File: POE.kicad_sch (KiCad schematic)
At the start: 9 parts, among them J1 Conn_01x02_Male

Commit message: ...
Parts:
- MOD-1: Footprint_1 Ag9912LP -> (none); Manufacturer_Part_Number Ag9912LP -> Ag9905LP; Mouser Part Number 480-AG9912LP -> (none); Mouser Price/Stock https://www.mouser.co.uk/ProductDetail/Silvertel/Ag9912LP?q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 -> (none); Reference_1 IC -> (none); Value_1 Ag9905LP -> (none)
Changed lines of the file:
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@@
       (effects (font (size 1.27 1.27)) hide)
-    )
-    (property "Reference_1" "IC" (id 4) (at 237.49 43.18 0))
-    (property "Value_1" "Ag9905LP" (id 5) (at 237.49 45.72 0))
-    (property "Footprint_1" "Ag9912LP" (id 6) (at 250.19 145.72 0)
-      (effects (font (size 1.27 1.27)) (justify left top) hide)
     )
     (property "Datasheet_1" "https://au.mouser.com/datasheet/2/1048/Ag9900M-datasheet-ultra-miniature-isolated-Power-o-1804309.pdf" (id 7) (at 250.19 245.72 0)
@@
       (effects (font (size 1.27 1.27)) (justify left top) hide)
     )
-    (property "Manufacturer_Part_Number" "Ag9912LP" (id 10) (at 250.19 645.72 0)
+    (property "Manufacturer_Part_Number" "Ag9905LP" (id 10) (at 250.19 645.72 0)
       (effects (font (size 1.27 1.27)) (justify left top) hide)
     )
-    (property "Mouser Part Number" "480-AG9912LP" (id 11) (at 250.19 745.72 0)
-      (effects (font (size 1.27 1.27)) (justify left top) hide)
-    )
-    (property "Mouser Price/Stock" "https://www.mouser.co.uk/ProductDetail/Silvertel/Ag9912LP?qs=OlC7AqGiEDllGSVQiYaPRA%3D%3D" (id 12) (at 250.19 845.72 0)
-      (effects (font (size 1.27 1.27)) (justify left top) hide)
-    )
-    (property "Arrow Part Number" "" (id 13) (at 250.19 945.72 0)
-      (effects (font (size 1.27 1.27)) (justify left top) hide)
-    )
-    (property "Arrow Price/Stock" "" (id 14) (at 250.19 1045.72 0)
-      (effects (font (size 1.27 1.27)) (justify left top) hide)
-    )

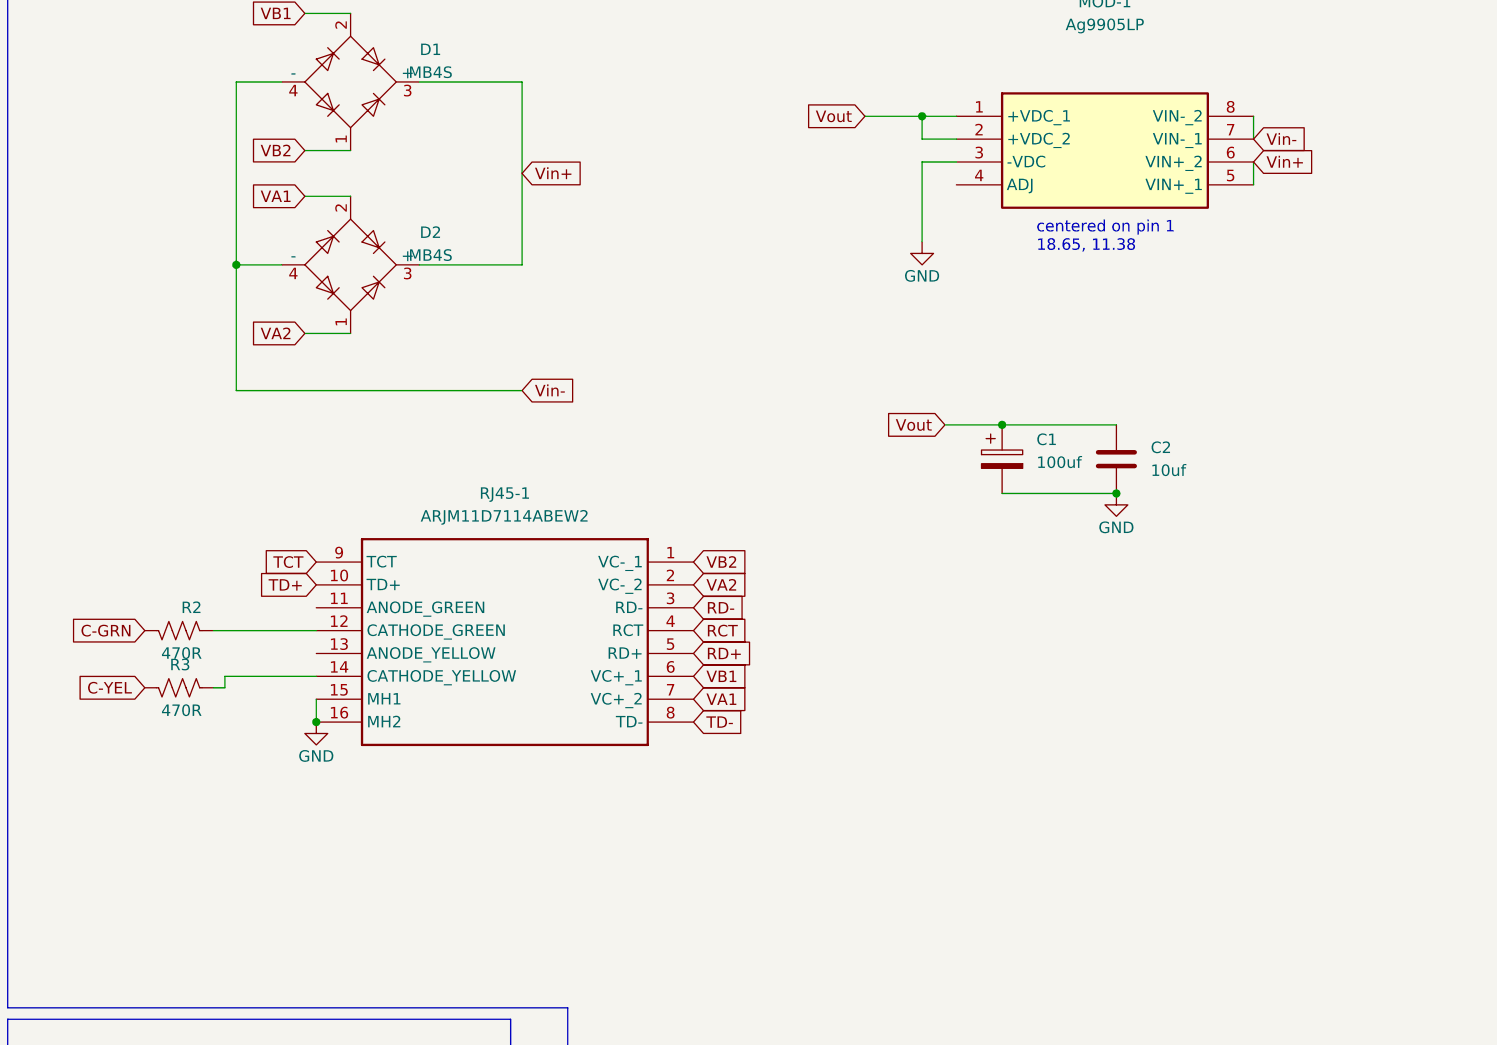
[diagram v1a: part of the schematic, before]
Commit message: Added adjustment & minLoad resistors
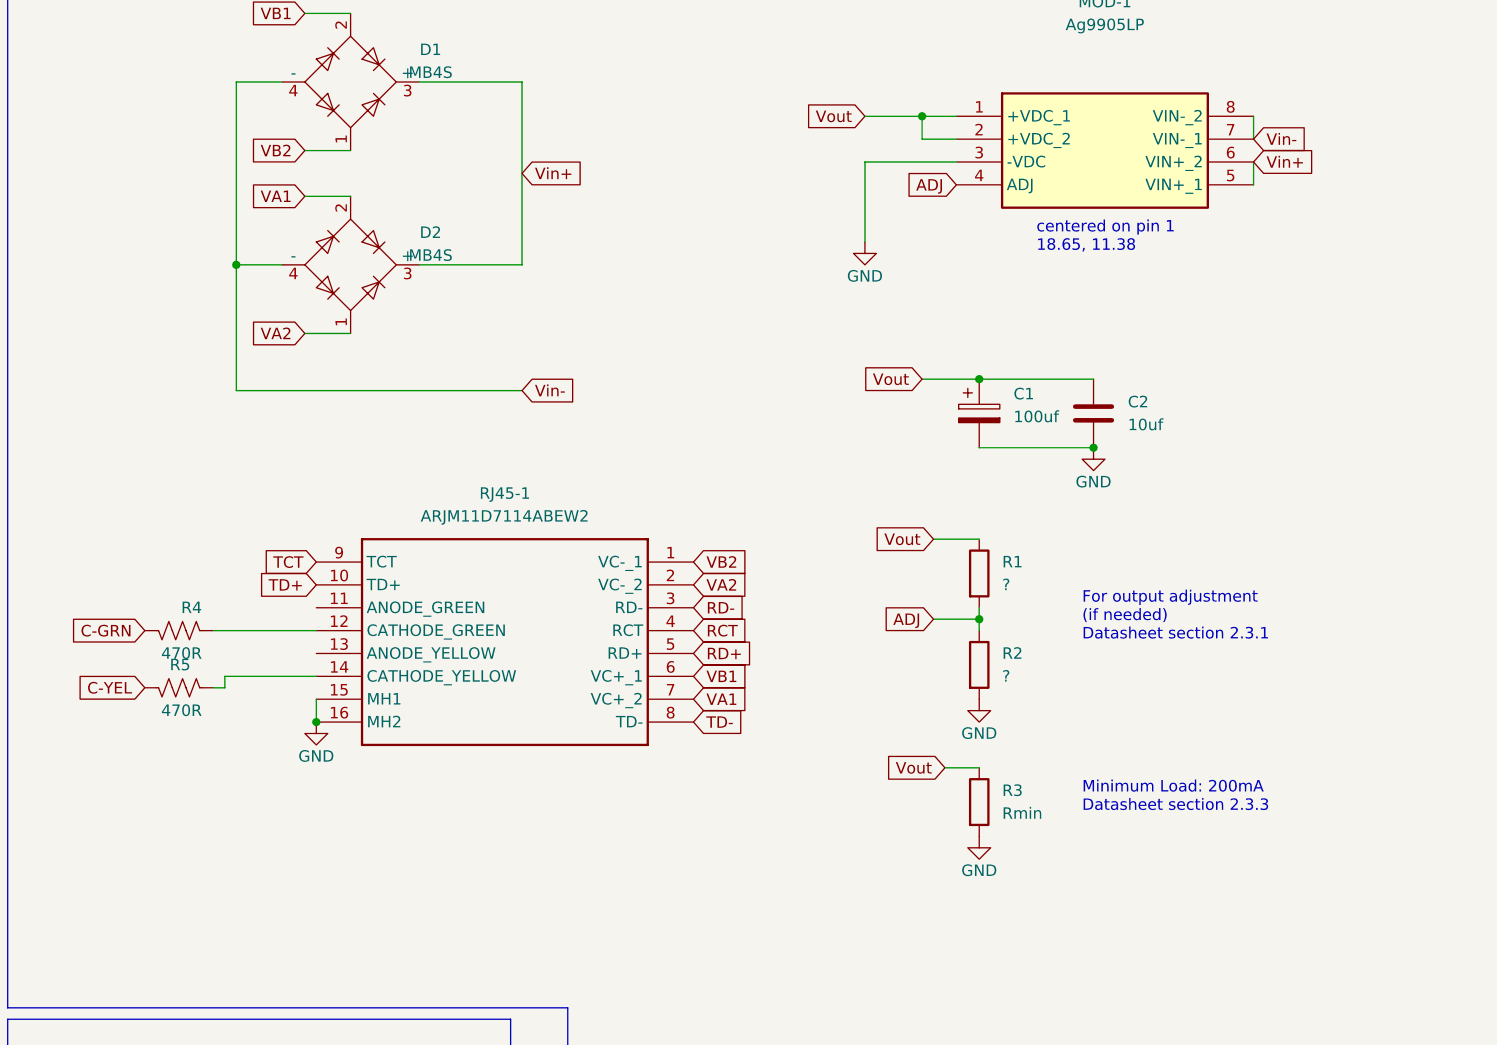
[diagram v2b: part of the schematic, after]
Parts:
- added R1, R2: ?, Resistor_SMD:R_0805_2012Metric_Pad1.20x1.40mm_HandSolder, symbol Device:R
- added R3: Rmin, Resistor_SMD:R_0805_2012Metric_Pad1.20x1.40mm_HandSolder, symbol Device:R
- renumbered R2 to R4, R3 to R5
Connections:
- net GND: now also R2.2, R3.2
- net Vout: now also R1.1, R3.1
- net ADJ: now reaches MOD-1.4 (ADJ)
- net ADJ: now also R1.2, R2.1
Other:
- note added: "For output adjustment (if needed) Datasheet section 2.3.1"
- note added: "Minimum Load: 200mA Datasheet section 2.3.3"
- moved on the sheet: C1, C2

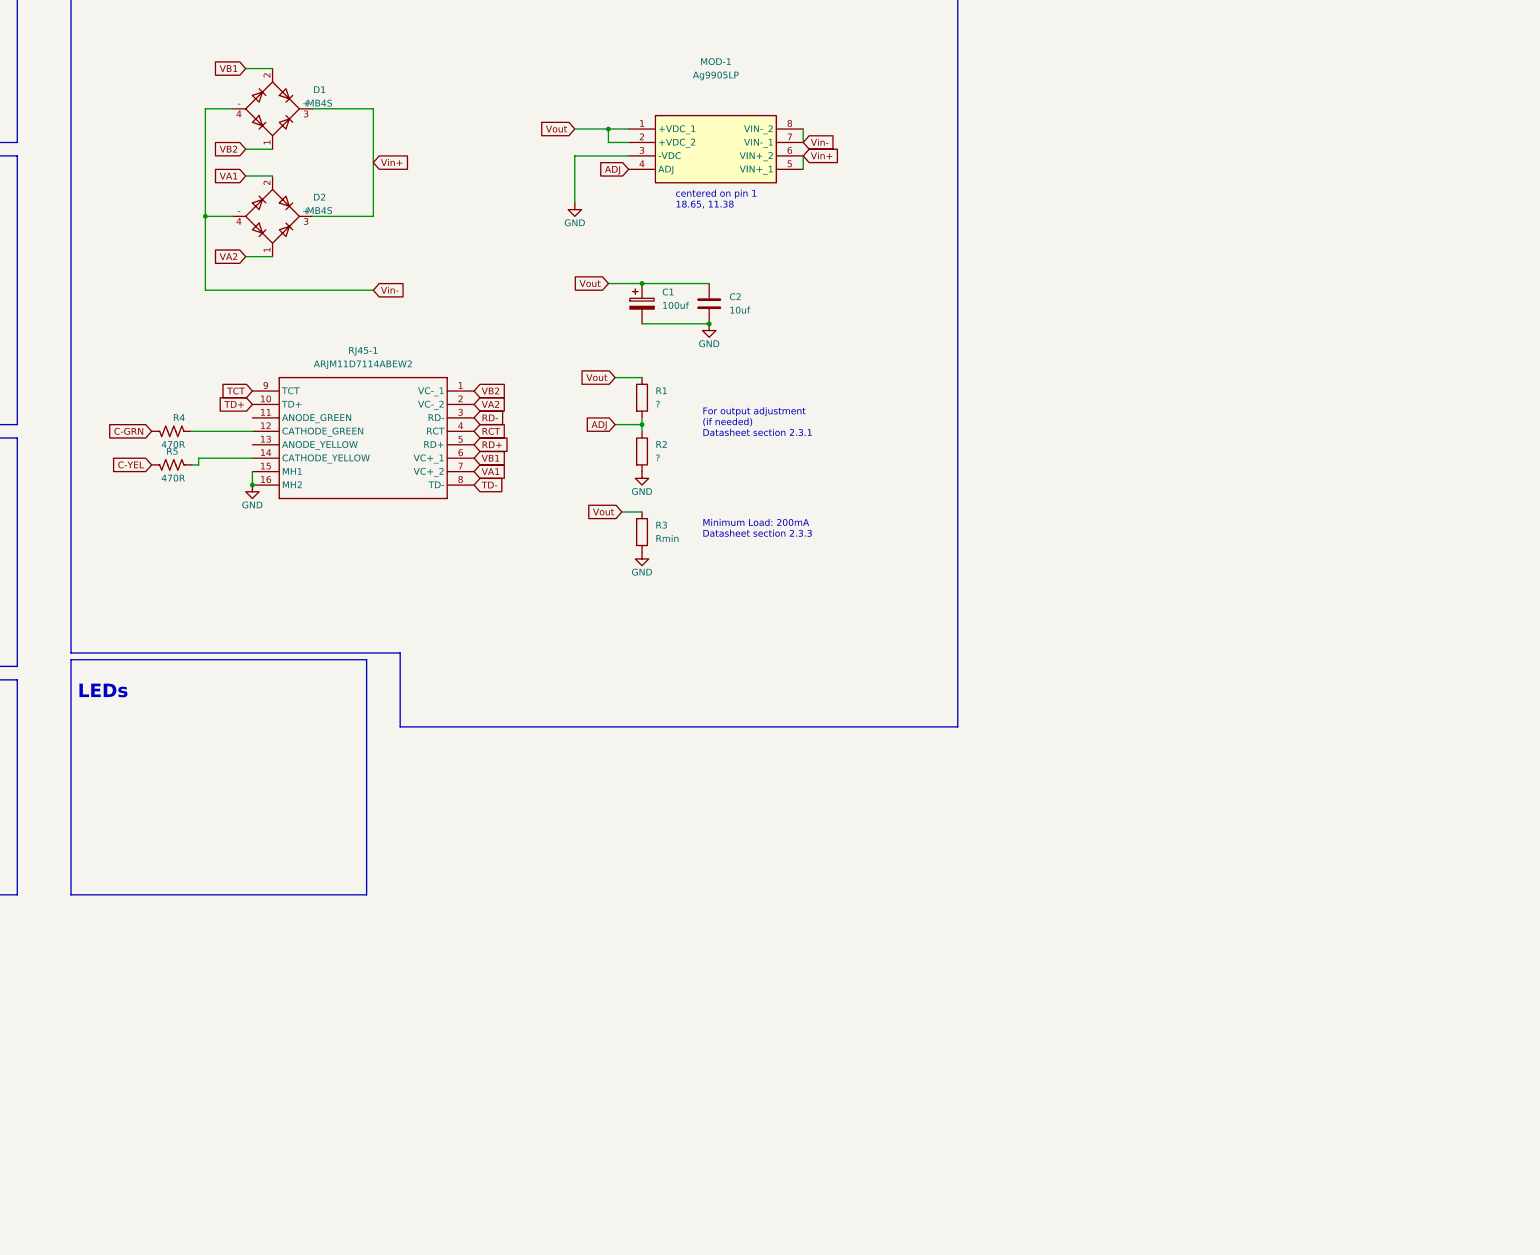
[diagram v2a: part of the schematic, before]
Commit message: upgraded from the overkill Ethernet jack to a better fit plus magnetics
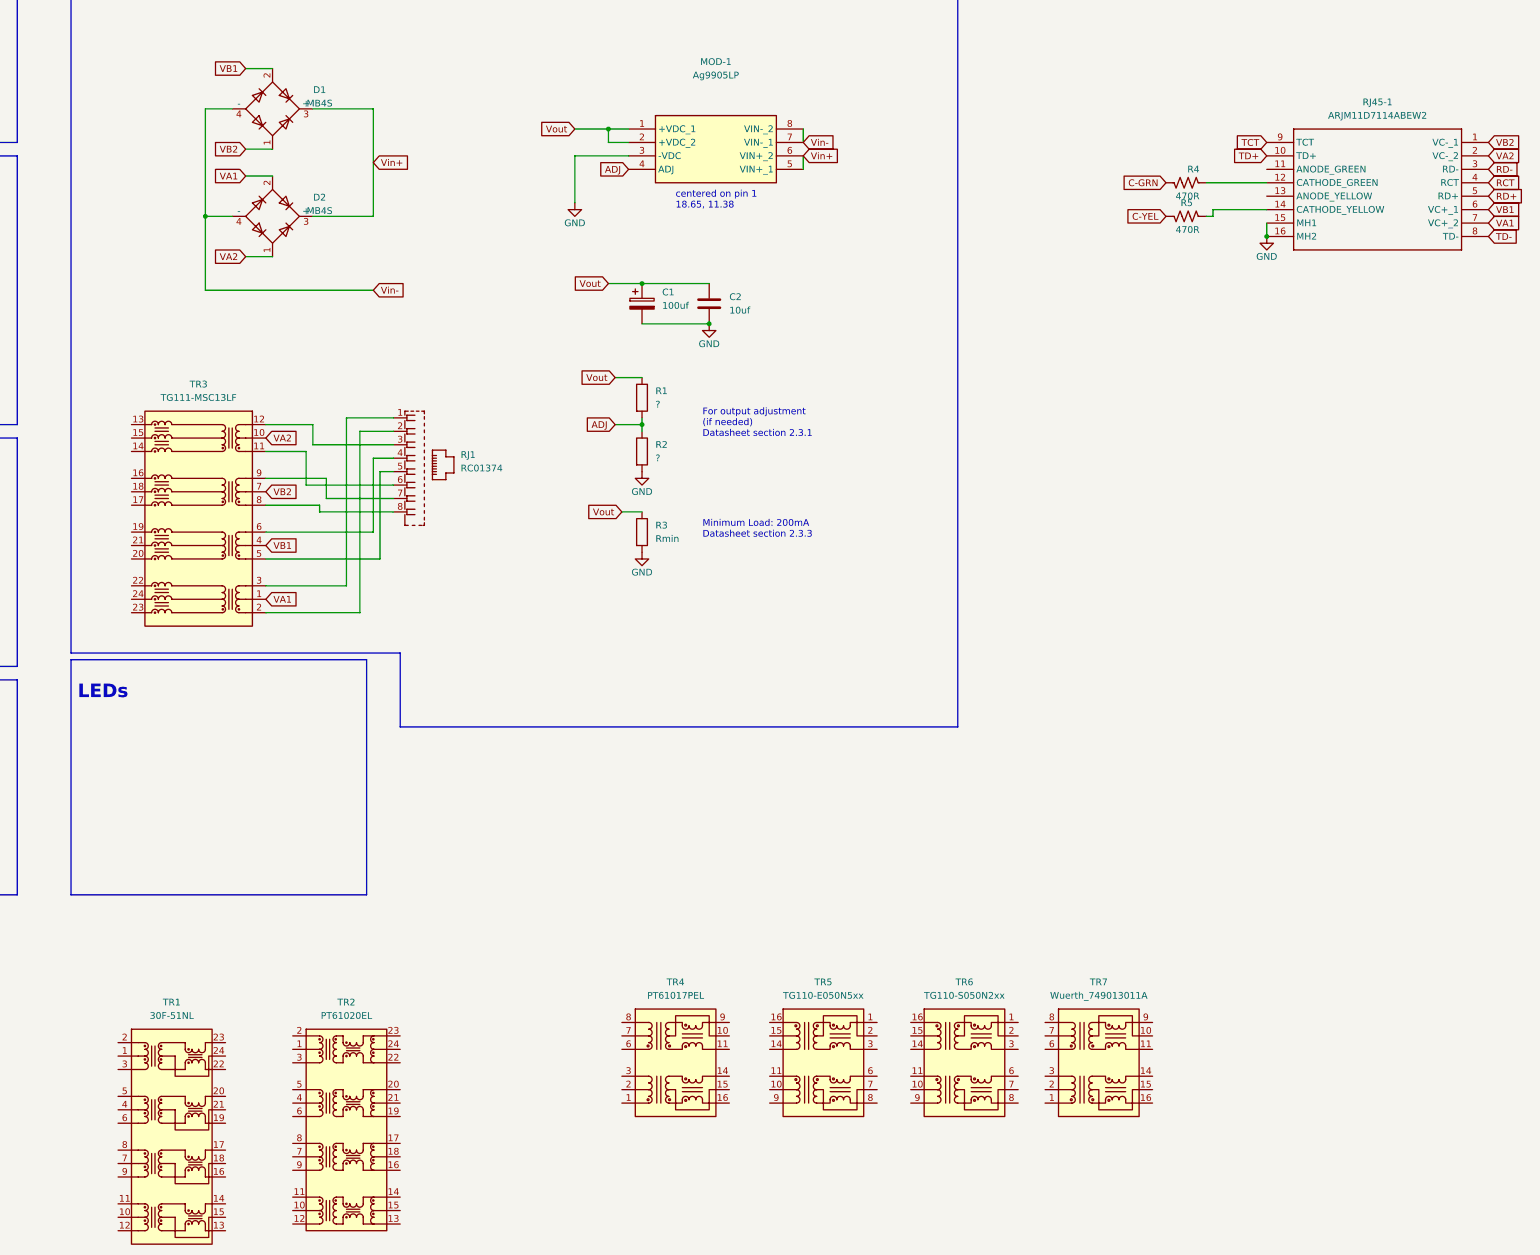
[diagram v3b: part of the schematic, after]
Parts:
- added RJ1: RC01374, tightstuff:RC01374, symbol Austins creations:RC01374
- added TR1: 30F-51NL, Transformer_SMD:Transformer_Ethernet_YDS_30F-51NL_SO-24_7.1x15.1mm, symbol Transformer:30F-51NL
- added TR2: PT61020EL, Transformer_SMD:Transformer_Ethernet_Bourns_PT61020EL, symbol Transformer:PT61020EL
- added TR3: TG111-MSC13LF, Transformer_SMD:Transformer_Ethernet_HALO_TG111-MSC13, symbol Transformer:TG111-MSC13LF
- added TR4: PT61017PEL, Transformer_SMD:Transformer_Ethernet_Bourns_PT61017PEL, symbol Transformer:PT61017PEL
- added TR5: TG110-E050N5xx, Transformer_SMD:Transformer_Ethernet_Halo_N5_SO-16_7.11x12.7mm, symbol Transformer:TG110-E050N5xx
- added TR6: TG110-S050N2xx, Transformer_SMD:Transformer_Ethernet_Halo_N2_SO-16_7.11x12.7mm, symbol Transformer:TG110-S050N2xx
- added TR7: Wuerth_749013011A, Transformer_SMD:Transformer_Ethernet_Wuerth_749013011A, symbol Transformer:Wuerth_749013011A
- RJ45-1: now left out of the parts list
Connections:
- net VA1: now also TR3.1 (TCT1)
- net VA2: now also TR3.10 (TCT4)
- net VB1: now also TR3.4 (TCT2)
- net VB2: now also TR3.7 (TCT3)
- new net: RJ1.6, TR3.11 (TD4+)
- new net: RJ1.3, TR3.12 (TD4-)
- new net: RJ1.2, TR3.2 (TD1+)
- new net: RJ1.1, TR3.3 (TD1-)
- new net: RJ1.5, TR3.5 (TD2+)
- new net: RJ1.4, TR3.6 (TD2-)
- new net: RJ1.8, TR3.8 (TD3+)
- new net: RJ1.7, TR3.9 (TD3-)
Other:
- moved on the sheet: R4, R5, RJ45-1

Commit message: Some layout rework...
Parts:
- removed R4, R5: 470R, Resistor_SMD:R_0603_1608Metric, symbol Device:R_US
- removed RJ45-1: ARJM11D7114ABEW2, Tinker:CONN_ARJM11D7-114-AB-EW2_ABR, symbol ARJM11D7-114-AB-EW2_ABR:ARJM11D7114ABEW2
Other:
- note added: "OR: SDAPO DP9900LP-5V"

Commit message: Improved Vout filtering
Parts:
- added C3: 10uf, Capacitor_SMD:C_0805_2012Metric, symbol Device:C
- added D3: SMAJ58A, Diode_SMD:D_SMA, symbol Diode:Z1SMAxxx
- added L1: fnr3015s1r, tightstuff:fnr3015s, symbol Device:L_Iron
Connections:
- net GND: now also J1.1 (Pin_1), C3.2; no longer J1.2 (Pin_2)
- net Vin+: now also D3.1 (K)
- net Vin-: now also D3.2 (A)
- net Vout: now also L1.1; no longer J1.1 (Pin_1)
- new net VoutF: C3.1, J1.2 (Pin_2), L1.2
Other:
- moved on the sheet: C1, C2, J1, RJ1, TR1, TR2, TR3, TR4, TR5, TR6, TR7

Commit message: foorprint improvements & parts selections...
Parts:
- removed TR1: 30F-51NL, Transformer_SMD:Transformer_Ethernet_YDS_30F-51NL_SO-24_7.1x15.1mm, symbol Transformer:30F-51NL
- removed TR2: PT61020EL, Transformer_SMD:Transformer_Ethernet_Bourns_PT61020EL, symbol Transformer:PT61020EL
- removed TR4: PT61017PEL, Transformer_SMD:Transformer_Ethernet_Bourns_PT61017PEL, symbol Transformer:PT61017PEL
- removed TR5: TG110-E050N5xx, Transformer_SMD:Transformer_Ethernet_Halo_N5_SO-16_7.11x12.7mm, symbol Transformer:TG110-E050N5xx
- removed TR6: TG110-S050N2xx, Transformer_SMD:Transformer_Ethernet_Halo_N2_SO-16_7.11x12.7mm, symbol Transformer:TG110-S050N2xx
- removed TR7: Wuerth_749013011A, Transformer_SMD:Transformer_Ethernet_Wuerth_749013011A, symbol Transformer:Wuerth_749013011A
- C1: footprint Capacitor_SMD:CP_Elec_5x3 -> Capacitor_SMD:CP_Elec_6.3x5.4
- TR3: value TG111-MSC13LF -> SET2401ST; footprint Transformer_SMD:Transformer_Ethernet_HALO_TG111-MSC13 -> tightstuff:Eth_Magnetics (1.0); LCSC (none) -> C7603464
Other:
- moved on the sheet: C1, C2, C3, J1, L1
